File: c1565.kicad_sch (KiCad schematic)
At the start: 7 parts, among them J4 Mini-DIN-8-With-Shield, U12 74LS125, U13 74LS125

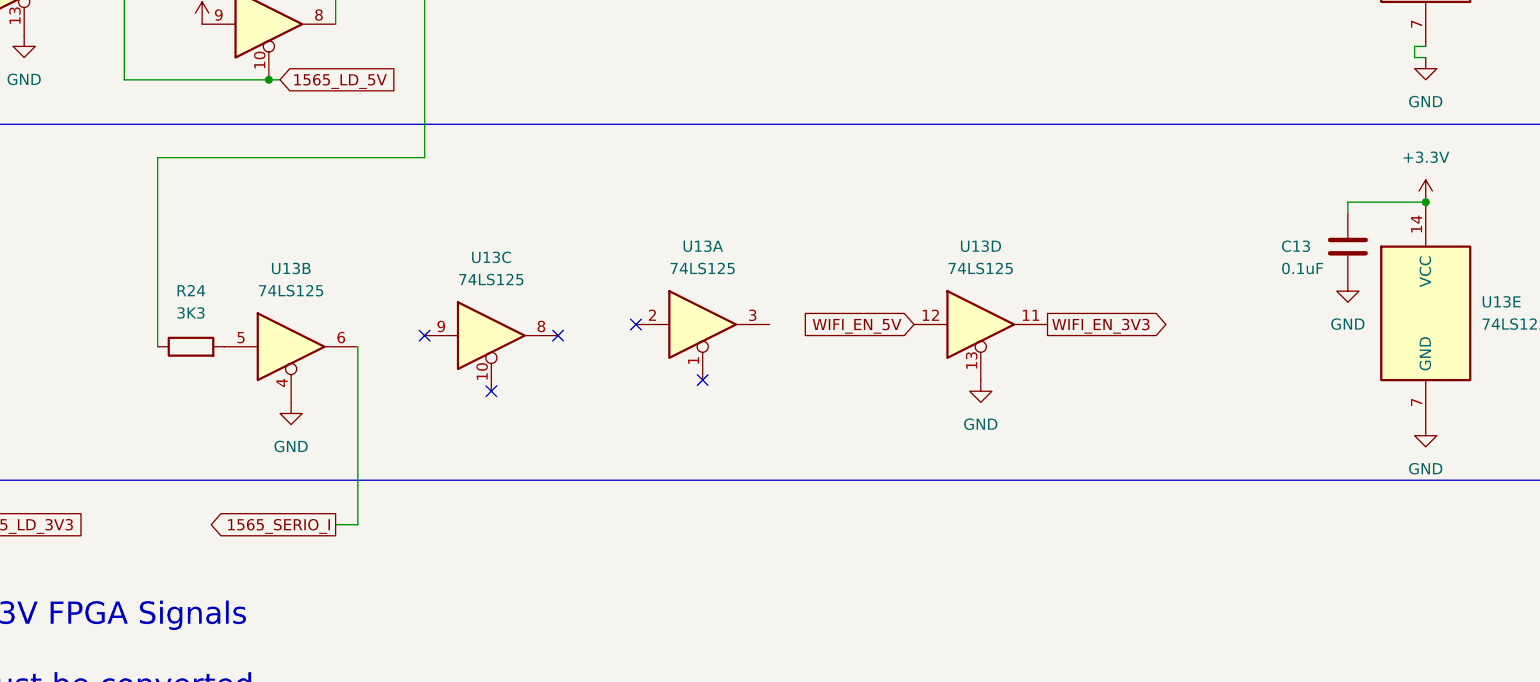
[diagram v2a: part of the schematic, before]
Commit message: document WIFI_EN, tidy up a bit more
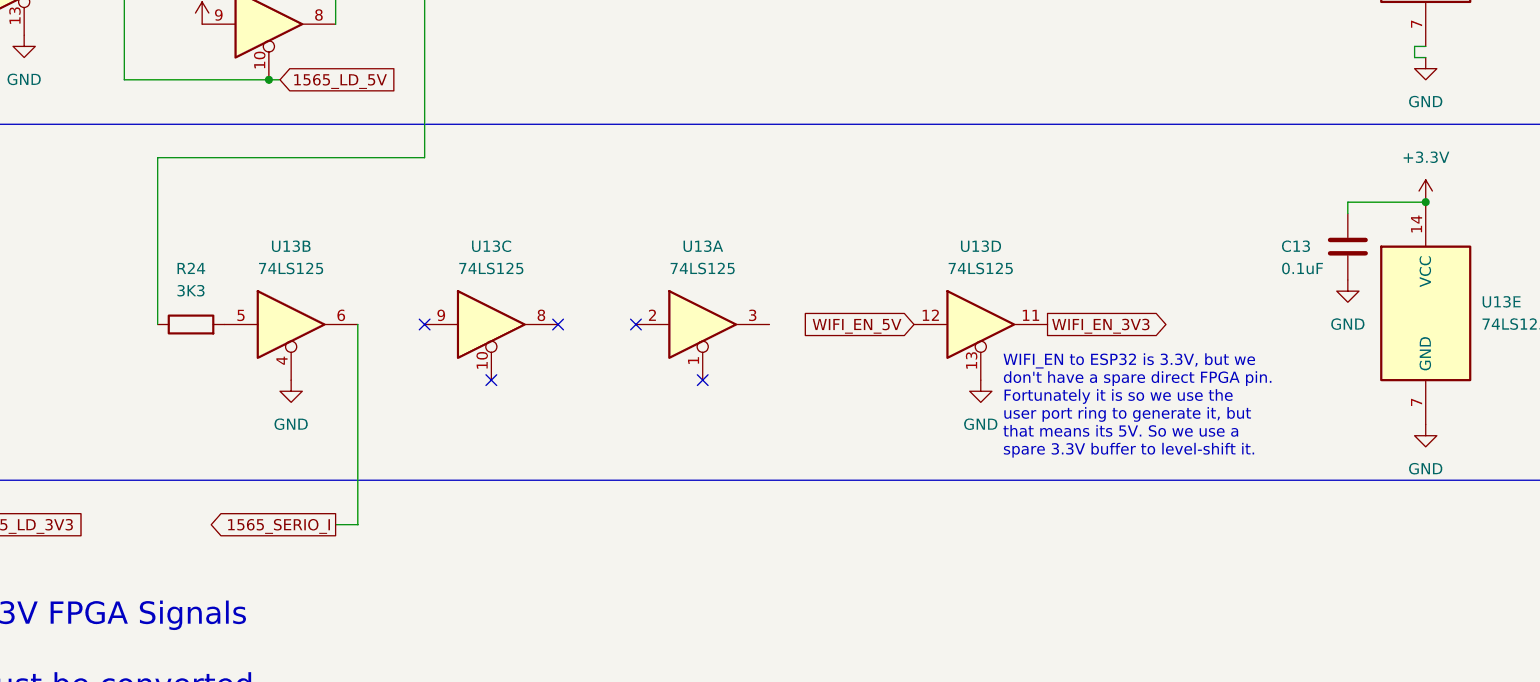
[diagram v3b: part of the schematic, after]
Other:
- note added: "WIFI_EN to ESP32 is 3.3V, but we don't have a spare direct FPGA pin. Fortunately it is so we use the user port ring to generate it, but that means its 5V. So we use a spare 3.3V buffer to level-shift it."
- moved on the sheet: R24, U13B, U13C
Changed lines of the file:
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@@
   )
   (no_connect (at 182.88 148.59))
-  (no_connect (at 151.13 143.51))
+  (no_connect (at 151.13 142.24))
   (no_connect (at 175.26 142.24))
-  (no_connect (at 158.75 149.86))
-  (no_connect (at 166.37 143.51))
+  (no_connect (at 158.75 148.59))
+  (no_connect (at 166.37 142.24))
   (wire (pts (xy 264.16 110.49) (xy 264.16 111.76))
     (stroke (width 0) (type default))
@@
     (stroke (width 0) (type default))
   )
-  (wire (pts (xy 143.51 165.1) (xy 143.51 144.78))
+  (wire (pts (xy 143.51 142.24) (xy 143.51 165.1))
     (stroke (width 0) (type default))
   )
@@
     (stroke (width 0) (type default))
   )
-  (wire (pts (xy 120.65 123.19) (xy 120.65 144.78))
+  (wire (pts (xy 120.65 123.19) (xy 120.65 142.24))
     (stroke (width 0) (type default))
   )
@@
     (effects (font (size 2.54 2.54)) (justify left bottom))
   )
+  (text "WIFI_EN to ESP32 is 3.3V, but we \ndon't have a spare direct FPGA pin.\nFortunately it is so we use the\nuser port ring to generate it, but\nthat means its 5V. So we use a \nspare 3.3V buffer to level-shift it."
+    (at 217.17 157.48 0)
+    (effects (font (size 1.27 1.27)) (justify left bottom))
+  )
   (label "C65 compatible C1565 External Drive Port" (at 190.5 190.5 0) (fields_autoplaced)
     (effects (font (size 1.27 1.27)) (justify left bottom))
@@
     )
   )
-  (symbol (lib_name "GND_1") (lib_id "power:GND") (at 135.89 151.13 0) (unit 1)
-    (in_bom yes) (on_board yes) (dnp no) (fields_autoplaced)
-    (property "Reference" "#PWR0106" (at 135.89 157.48 0)
-      (effects (font (size 1.27 1.27)) hide)
-    )
-    (property "Value" "GND" (at 135.89 156.21 0)
-      (effects (font (size 1.27 1.27)))
-    )
-    (property "Footprint" "" (at 135.89 151.13 0)
-      (effects (font (size 1.27 1.27)) hide)
-    )
-    (property "Datasheet" "" (at 135.89 151.13 0)
+  (symbol (lib_name "GND_1") (lib_id "power:GND") (at 135.89 148.59 0) (unit 1)
+    (in_bom yes) (on_board yes) (dnp no) (fields_autoplaced)
+    (property "Reference" "#PWR0106" (at 135.89 154.94 0)
+      (effects (font (size 1.27 1.27)) hide)
+    )
+    (property "Value" "GND" (at 135.89 153.67 0)
+      (effects (font (size 1.27 1.27)))
+    )
+    (property "Footprint" "" (at 135.89 148.59 0)
+      (effects (font (size 1.27 1.27)) hide)
+    )
+    (property "Datasheet" "" (at 135.89 148.59 0)
       (effects (font (size 1.27 1.27)) hide)
     )
@@
     )
   )
-  (symbol (lib_id "74xx:74LS125") (at 158.75 143.51 0) (unit 3)
-    (in_bom yes) (on_board yes) (dnp no) (fields_autoplaced)
-    (property "Reference" "U13" (at 158.75 134.62 0)
-      (effects (font (size 1.27 1.27)))
-    )
-    (property "Value" "74LS125" (at 158.75 137.16 0)
-      (effects (font (size 1.27 1.27)))
-    )
-    (property "Footprint" "snapeda:DIP-14_74LS06" (at 158.75 143.51 0)
-      (effects (font (size 1.27 1.27)) hide)
-    )
-    (property "Datasheet" "http://www.ti.com/lit/gpn/sn74LS125" (at 158.75 143.51 0)
+  (symbol (lib_id "74xx:74LS125") (at 158.75 142.24 0) (unit 3)
+    (in_bom yes) (on_board yes) (dnp no) (fields_autoplaced)
+    (property "Reference" "U13" (at 158.75 133.35 0)
+      (effects (font (size 1.27 1.27)))
+    )
+    (property "Value" "74LS125" (at 158.75 135.89 0)
+      (effects (font (size 1.27 1.27)))
+    )
+    (property "Footprint" "snapeda:DIP-14_74LS06" (at 158.75 142.24 0)
+      (effects (font (size 1.27 1.27)) hide)
+    )
+    (property "Datasheet" "http://www.ti.com/lit/gpn/sn74LS125" (at 158.75 142.24 0)
       (effects (font (size 1.27 1.27)) hide)
     )
@@
     )
   )
-  (symbol (lib_id "74xx:74LS125") (at 135.89 144.78 0) (unit 2)
-    (in_bom yes) (on_board yes) (dnp no) (fields_autoplaced)
-    (property "Reference" "U13" (at 135.89 135.89 0)
-      (effects (font (size 1.27 1.27)))
-    )
-    (property "Value" "74LS125" (at 135.89 138.43 0)
-      (effects (font (size 1.27 1.27)))
-    )
-    (property "Footprint" "snapeda:DIP-14_74LS06" (at 135.89 144.78 0)
-      (effects (font (size 1.27 1.27)) hide)
-    )
-    (property "Datasheet" "http://www.ti.com/lit/gpn/sn74LS125" (at 135.89 144.78 0)
+  (symbol (lib_id "74xx:74LS125") (at 135.89 142.24 0) (unit 2)
+    (in_bom yes) (on_board yes) (dnp no) (fields_autoplaced)
+    (property "Reference" "U13" (at 135.89 133.35 0)
+      (effects (font (size 1.27 1.27)))
+    )
+    (property "Value" "74LS125" (at 135.89 135.89 0)
+      (effects (font (size 1.27 1.27)))
+    )
+    (property "Footprint" "snapeda:DIP-14_74LS06" (at 135.89 142.24 0)
+      (effects (font (size 1.27 1.27)) hide)
+    )
+    (property "Datasheet" "http://www.ti.com/lit/gpn/sn74LS125" (at 135.89 142.24 0)
       (effects (font (size 1.27 1.27)) hide)
     )
@@
     )
   )
-  (symbol (lib_id "Device:R") (at 124.46 144.78 90) (unit 1)
-    (in_bom yes) (on_board yes) (dnp no) (fields_autoplaced)
-    (property "Reference" "R24" (at 124.46 138.43 90)
-      (effects (font (size 1.27 1.27)))
-    )
-    (property "Value" "3K3" (at 124.46 140.97 90)
-      (effects (font (size 1.27 1.27)))
-    )
-    (property "Footprint" "snapeda:Labeled Resistor" (at 124.46 146.558 90)
-      (effects (font (size 1.27 1.27)) hide)
-    )
-    (property "Datasheet" "~" (at 124.46 144.78 0)
-      (effects (font (size 1.27 1.27)) hide)
-    )
+  (symbol (lib_id "Device:R") (at 124.46 142.24 90) (unit 1)
+    (in_bom yes) (on_board yes) (dnp no) (fields_autoplaced)
+    (property "Reference" "R24" (at 124.46 135.89 90)
+      (effects (font (size 1.27 1.27)))
+    )
+    (property "Value" "3K3" (at 124.46 138.43 90)
+      (effects (font (size 1.27 1.27)))
+    )
+    (property "Footprint" "snapeda:Labeled Resistor" (at 124.46 144.018 90)
+      (effects (font (size 1.27 1.27)) hide)
+    )
+    (property "Datasheet" "~" (at 124.46 142.24 0)
+      (effects (font (size 1.27 1.27)) hide)
+    )

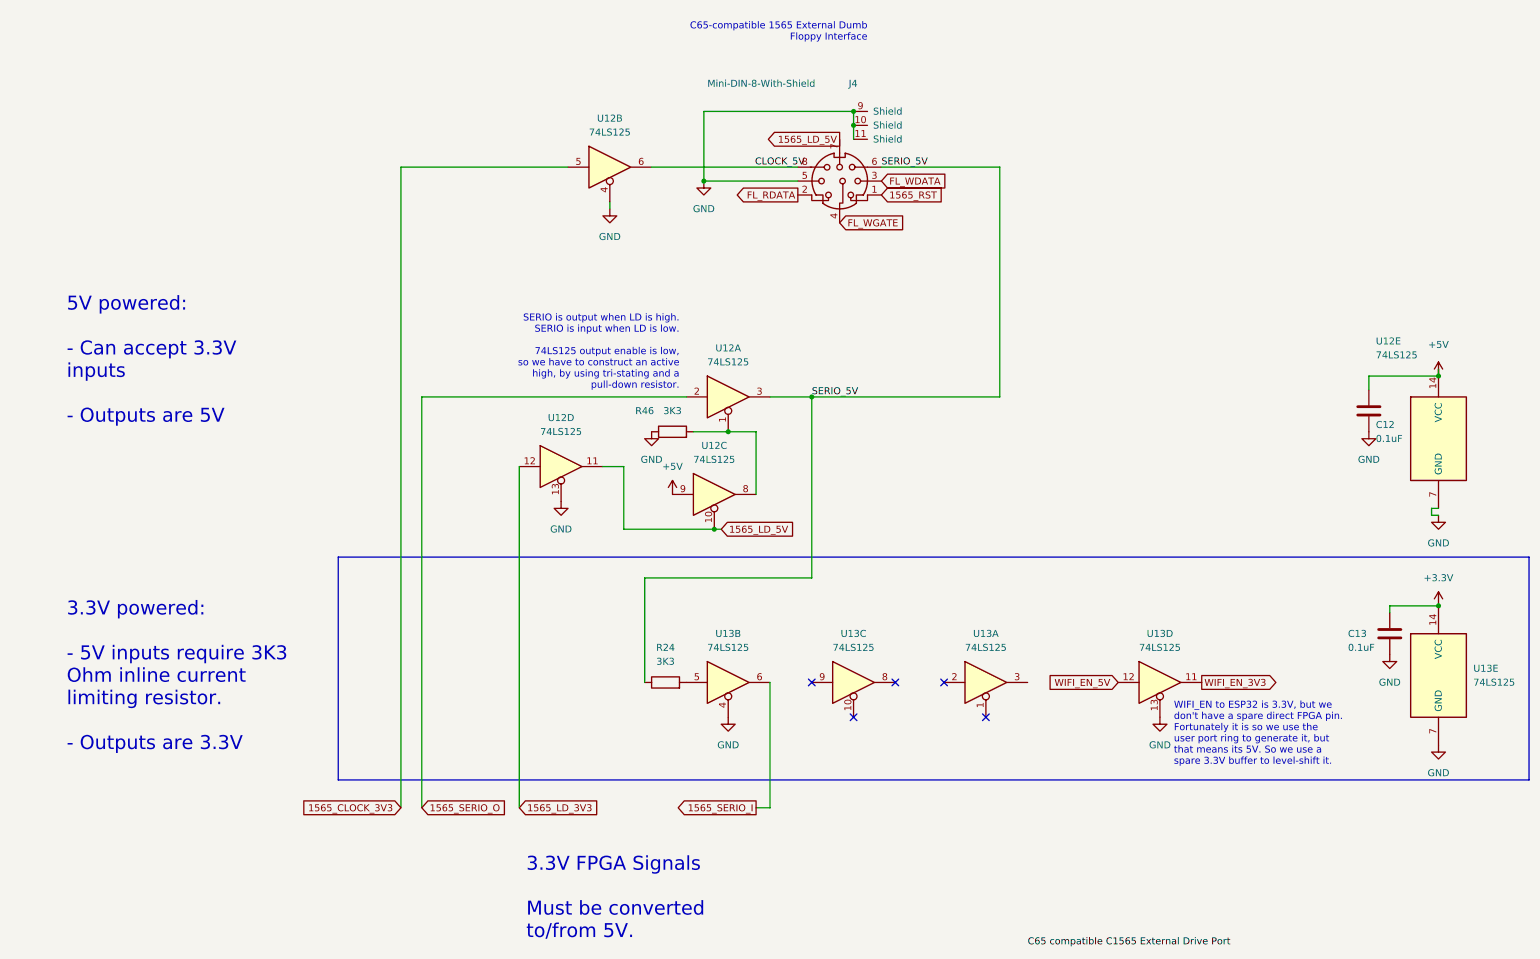
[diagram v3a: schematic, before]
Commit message: add A/V filter circuits and audio links to bridge board
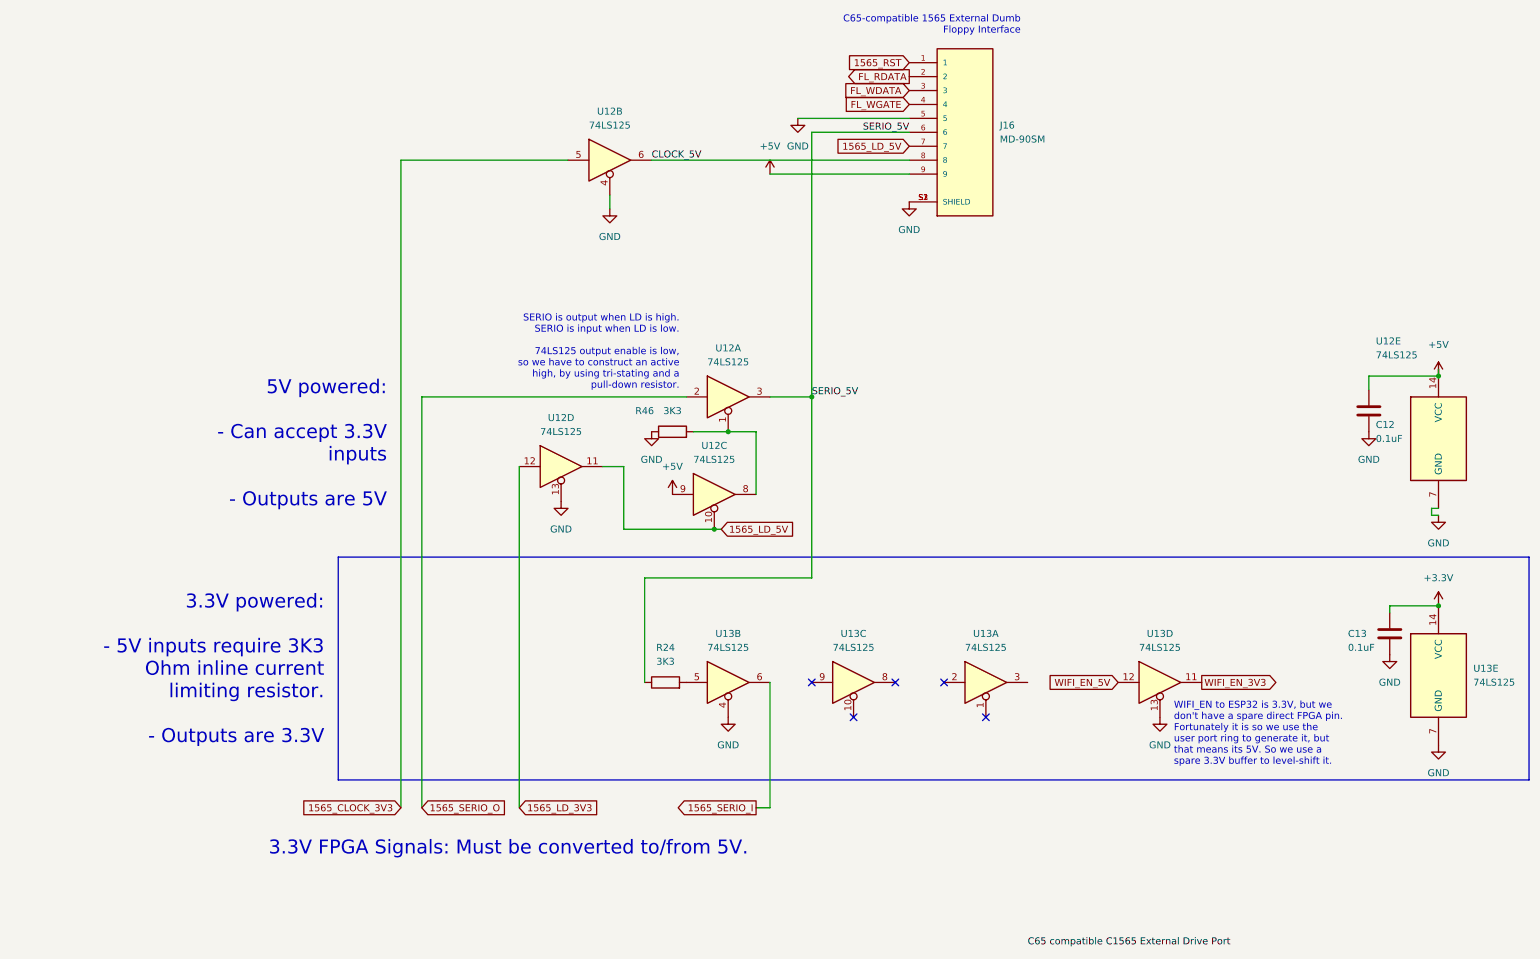
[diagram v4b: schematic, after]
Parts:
- removed J4: Mini-DIN-8-With-Shield, snapeda:mini-DIN-8, symbol 00Project-SDF-60J:Mini-DIN-8-With-Shield
- added J16: MD-90SM, snapeda:CUI_MD-90SM, symbol 00Project-MD90:MD-90SM
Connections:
- net +5V: now also J16.9
- net 1565_LD_5V: now also J16.7
- net 1565_RST: now also J16.1
- net CLOCK_5V: now also U12.6, J16.8
- net FL_RDATA: now also J16.2
- net FL_WDATA: now also J16.3
- net FL_WGATE: now also J16.4
- net GND: now also J16.5, J16.S1 (SHIELD), J16.S2 (SHIELD), J16.S3 (SHIELD)
- net SERIO_5V: now also J16.6
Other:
- note added: "3.3V FPGA Signals: Must be converted to/from 5V."
- note removed: "3.3V FPGA Signals Must be converted to/from 5V."
- moved on the sheet: U12B

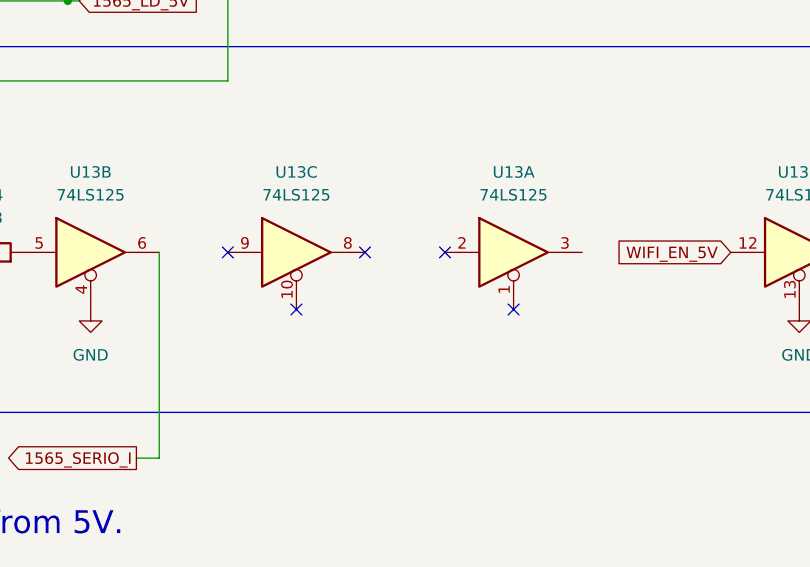
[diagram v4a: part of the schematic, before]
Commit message: fix floating gate inputs
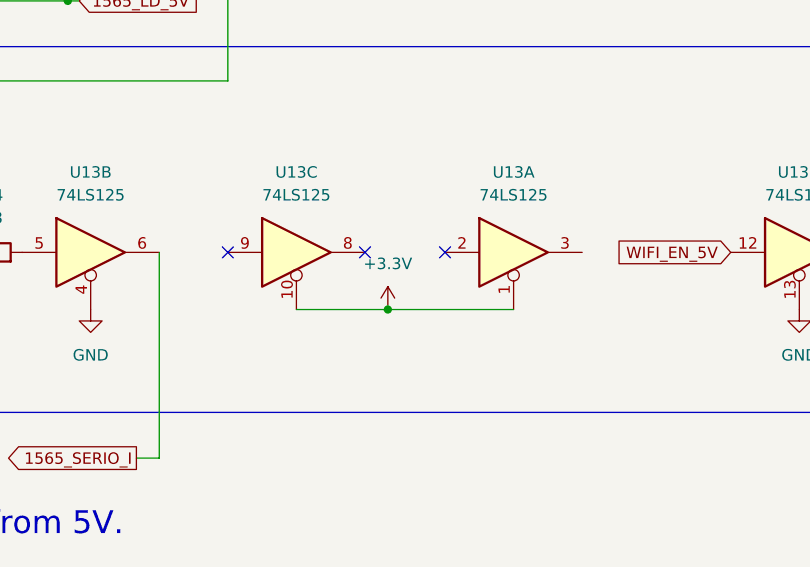
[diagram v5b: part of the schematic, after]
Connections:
- net +3V3: now also U13.1, U13.10
- no-connect marks 5 -> 3
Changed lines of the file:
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@@
   (junction (at 135.89 96.52) (diameter 0) (color 0 0 0 0)
   )
+  (junction (at 168.91 148.59) (diameter 0) (color 0 0 0 0)
+  )
   (junction (at 265.43 86.36) (diameter 0) (color 0 0 0 0)
   )
-  (no_connect (at 182.88 148.59))
   (no_connect (at 151.13 142.24))
   (no_connect (at 175.26 142.24))
-  (no_connect (at 158.75 148.59))
   (no_connect (at 166.37 142.24))
   (wire (pts (xy 143.51 49.53) (xy 168.91 49.53))
@@
     (stroke (width 0) (type default))
   )
+  (wire (pts (xy 168.91 148.59) (xy 182.88 148.59))
+    (stroke (width 0) (type default))
+  )
   (wire (pts (xy 80.01 90.17) (xy 80.01 165.1))
     (stroke (width 0) (type default))
@@
   )
   (wire (pts (xy 256.54 128.27) (xy 265.43 128.27))
+    (stroke (width 0) (type default))
+  )
+  (wire (pts (xy 158.75 148.59) (xy 168.91 148.59))
     (stroke (width 0) (type default))
   )
@@
         )
       )
+    )
+  )
+  (symbol (lib_id "power:+3.3V") (at 168.91 148.59 0) (unit 1)
+    (in_bom yes) (on_board yes) (dnp no) (fields_autoplaced)
+    (property "Reference" "#PWR0118" (at 168.91 152.4 0)
+      (effects (font (size 1.27 1.27)) hide)
+    )
+    (property "Value" "+3.3V" (at 168.91 143.51 0)
+      (effects (font (size 1.27 1.27)))
+    )
+    (property "Footprint" "" (at 168.91 148.59 0)
+      (effects (font (size 1.27 1.27)) hide)
+    )
+    (property "Datasheet" "" (at 168.91 148.59 0)
+      (effects (font (size 1.27 1.27)) hide)
+    )
+    (pin "1")
+    (instances
+      (project "mega65-r3-expansion-board.kicad"
+        (path "/e63e39d7-6ac0-4ffd-8aa3-1841a4541b55/146a8bef-6809-4ca3-9c51-e7afef5be129"
+          (reference "#PWR0118") (unit 1)
+        )
+      )
